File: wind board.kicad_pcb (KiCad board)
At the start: 2 copper layers, 50 x 50 mm, 63 parts, among them J1 USB_C_Receptacle_USB2.0_14P, J2 Conn_01x06_MountingPin, J3 Conn_01x06_MountingPin, U1 CH334R, U2 FT232RL, U3 FT232RL, U4 ZT3222F, U5 ZT3222F, Y1 12MHz

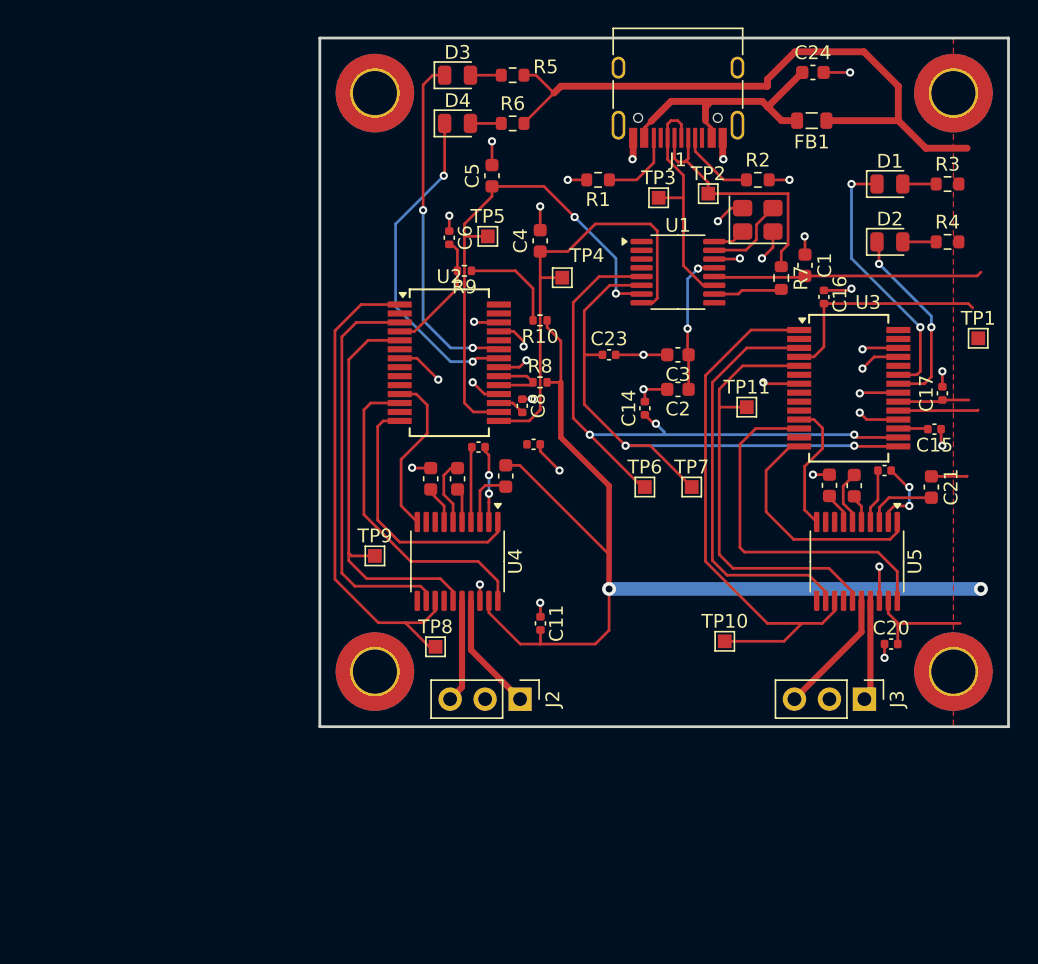
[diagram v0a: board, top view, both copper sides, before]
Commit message: added 3rd interface, tvs diodes, charging circuit
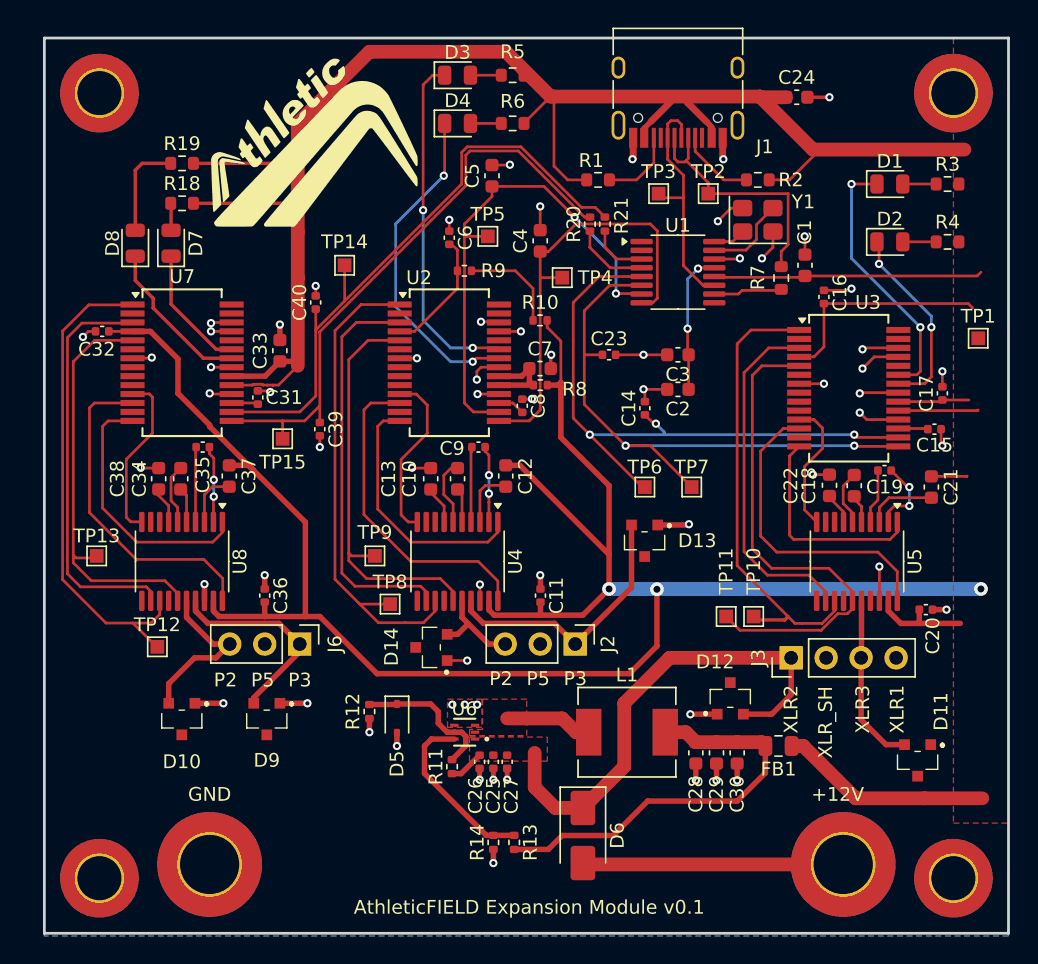
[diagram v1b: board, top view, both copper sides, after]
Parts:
- added C25: 10µF, Capacitor_SMD:C_0402_1005Metric, F.Cu at (131.6, 102.5)
- added C26: 10µF, Capacitor_SMD:C_0402_1005Metric, F.Cu at (130.6, 102.5)
- added C27: 0.1µF, Capacitor_SMD:C_0402_1005Metric, F.Cu at (132.6, 102.5)
- added C28: 22µF, Capacitor_SMD:C_0603_1608Metric, F.Cu at (146.3, 101.9)
- added C29: 22µF, Capacitor_SMD:C_0603_1608Metric, F.Cu at (147.8, 101.9)
- added C30: 22µF, Capacitor_SMD:C_0603_1608Metric, F.Cu at (149.3, 101.9)
- added C31: 100nF, Capacitor_SMD:C_0402_1005Metric, F.Cu at (114.5, 76.1)
- added C32: 100nF, Capacitor_SMD:C_0402_1005Metric, F.Cu at (103.2, 71.3)
- added C33: 4.7µF, Capacitor_SMD:C_0603_1608Metric, F.Cu at (116.1, 72.7)
- added C34: 470nF, Capacitor_SMD:C_0603_1608Metric, F.Cu at (108.9, 82.0)
- added C35: 100nF, Capacitor_SMD:C_0402_1005Metric, F.Cu at (110.5, 79.7)
- added C36: 100nF, Capacitor_SMD:C_0402_1005Metric, F.Cu at (115.0, 90.5)
- added C37: 470nF, Capacitor_SMD:C_0603_1608Metric, F.Cu at (112.4, 81.8)
- added C38: 470nF, Capacitor_SMD:C_0603_1608Metric, F.Cu at (107.3, 82.0)
- added C39: 47pF, Capacitor_SMD:C_0402_1005Metric, F.Cu at (119.0, 78.4)
- added C40: 47pF, Capacitor_SMD:C_0402_1005Metric, F.Cu at (118.7, 69.2)
- added D10: SM15-02HTG, Package_TO_SOT_SMD:SM0502HTG, F.Cu at (109.0, 99.4)
- added D11: SM15-02HTG, Package_TO_SOT_SMD:SM0502HTG, F.Cu at (162.4, 102.4)
- added D12: SM15-02HTG, Package_TO_SOT_SMD:SM0502HTG, F.Cu at (148.8, 97.9)
- added D13: SM15-02HTG, Package_TO_SOT_SMD:SM0502HTG, F.Cu at (142.6, 86.5)
- added D14: SM15-02HTG, Package_TO_SOT_SMD:SM0502HTG, F.Cu at (127.1, 94.2)
- added D5: 1N4148WS, Diode_SMD:D_SOD-323, F.Cu at (124.6, 99.4)
- added D6: SS54, Diode_SMD:D_SMA, F.Cu at (138.1, 107.9)
- added D7: LED, LED_SMD:LED_0805_2012Metric, F.Cu at (108.2, 64.9)
- added D8: LED, LED_SMD:LED_0805_2012Metric, F.Cu at (105.6, 64.9)
- added D9: SM15-02HTG, Package_TO_SOT_SMD:SM0502HTG, F.Cu at (115.2, 99.4)
- added G***: LOGO, logos:athletic Square, F.Cu at (118.6, 57.6)
- added J4: 12V -, MountingHole:MountingHole_4.3mm_M4_ISO7380_Pad_TopBottom, F.Cu at (111.0, 110.0)
- added J5: 12V +, MountingHole:MountingHole_4.3mm_M4_ISO7380_Pad_TopBottom, F.Cu at (157.0, 110.0)
- added J6: Conn_01x06_MountingPin, Connector_PinHeader_2.54mm:PinHeader_1x03_P2.54mm_Vertical, F.Cu at (117.5, 94.0)
- added L1: SPM6530T-2R2M, Inductor_SMD:IND_SPM6530T-2R2M, F.Cu at (141.3, 100.4)
- added R11: 20KΩ, Resistor_SMD:R_0402_1005Metric, F.Cu at (128.6, 102.9)
- added R12: 30KΩ, Resistor_SMD:R_0402_1005Metric, F.Cu at (122.6, 98.9)
- added R13: 220KΩ, Resistor_SMD:R_0402_1005Metric, F.Cu at (133.1, 108.4)
- added R14: 30KΩ, Resistor_SMD:R_0402_1005Metric, F.Cu at (131.6, 108.4)
- added R18: 470Ω, Resistor_SMD:R_0603_1608Metric, F.Cu at (109.0, 62.0)
- added R19: 470Ω, Resistor_SMD:R_0603_1608Metric, F.Cu at (109.0, 59.1)
- added R20: 0Ω, Resistor_SMD:R_0402_1005Metric, F.Cu at (138.6, 63.5)
- added R21: 0Ω, Resistor_SMD:R_0402_1005Metric, F.Cu at (139.7, 63.5)
- added TP12: TestPoint, TestPoint:TestPoint_Pad_1.0x1.0mm, F.Cu at (107.2, 94.2)
- added TP13: TestPoint, TestPoint:TestPoint_Pad_1.0x1.0mm, F.Cu at (102.8, 87.6)
- added TP14: TestPoint, TestPoint:TestPoint_Pad_1.0x1.0mm, F.Cu at (120.8, 66.5)
- added TP15: TestPoint, TestPoint:TestPoint_Pad_1.0x1.0mm, F.Cu at (116.3, 79.1)
- added U6: TPS565242, Package_TO_SOT_SMD:SOT6_DRL_TEX-L, F.Cu at (129.5, 100.4)
- added U7: FT232RL, Package_SO:SSOP-28_5.3x10.2mm_P0.65mm, F.Cu at (109.0, 73.6)
- added U8: ZT3222F, Package_SO:TSSOP-20_4.4x6.5mm_P0.65mm, F.Cu at (109.0, 88.0)
- C7: footprint Capacitor_SMD:C_0402_1005Metric -> Capacitor_SMD:C_0603_1608Metric
- FB1: value 600R/0.5A -> 600R/3A; footprint Inductor_SMD:L_0805_2012Metric -> Capacitor_SMD:C_0805_2012Metric
- J3: footprint Connector_PinHeader_2.54mm:PinHeader_1x03_P2.54mm_Vertical -> Connector_PinHeader_2.54mm:PinHeader_1x04_P2.54mm_Vertical
- R1, R2: value 5.1KΩ -> 22KΩ
- moved FB1 45.5 mm to (152.3, 101.4)
- moved REF** 25.0 mm to (103.0, 111.0)
- moved REF** 20.0 mm to (103.0, 54.0)
- moved TP11 15.3 mm to (148.5, 92.0)
- moved REF** 15.0 mm to (165.0, 111.0)
- moved J3 6.11 mm to (153.2, 95.0), turned to 90 degrees
- moved J2 5.66 mm to (137.5, 94.0)
- moved C7 5.52 mm to (135.0, 74.0)
- moved TP8 4.53 mm to (124.1, 91.1)
- moved C20 3.55 mm to (163.0, 91.5), turned to 180 degrees
- moved TP10 2.77 mm to (150.5, 92.0)
- moved C24 2.15 mm to (153.6, 54.3)
- moved C11 2.02 mm to (135.0, 90.5)
- moved TP3 0.30 mm to (143.6, 61.3)
- moved R8 0.20 mm to (135.0, 75.2)
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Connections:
- net +3.3V renamed Net-(U1-VDD33)
- C24 pad 1: Net-(C24-Pad1) -> +5V
- FB1 pad 2: Net-(C24-Pad1) -> Net-(C28-Pad1)
- J1 pad A4: Net-(C24-Pad1) -> +5V
- J1 pad A9: Net-(C24-Pad1) -> +5V
- J1 pad B4: Net-(C24-Pad1) -> +5V
- J1 pad B9: Net-(C24-Pad1) -> +5V
- J3 pad 1: Net-(J3-Pin_1) -> /WG_+12V
- R1 pad 1: Net-(J1-CC2) -> +5V
- R1 pad 2: ~ -> Net-(J1-CC2)
- R2 pad 1: Net-(J1-CC1) -> +5V
- R2 pad 2: ~ -> Net-(J1-CC1)
- U1 pad 3: unconnected-(U1-DM3--Pad3) -> /DM3-
- U1 pad 4: unconnected-(U1-DP3+-Pad4) -> /DM3+
- U5 pad 17: Net-(J3-Pin_1) -> unconnected-(U5-T1OUT-Pad17)
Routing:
- net +5V: track 178.7 -> 337.9 mm, vias 2 -> 3
- net Net-(U7-USBD-): track 0.00 -> 45.5 mm
- net Net-(U7-USBD+): track 0.00 -> 43.1 mm
- net /WG_+12V: track 0.00 -> 38.3 mm
- net Net-(U7-TXD): track 0.00 -> 35.6 mm
- net Net-(C28-Pad1): track 0.00 -> 30.0 mm
- net Net-(U7-RXD): track 0.00 -> 29.3 mm
- net Net-(U7-RTS): track 0.00 -> 28.5 mm
- net ~: track 68.7 -> 93.0 mm, vias 35 -> 63
- net Net-(U7-CBUS4): track 0.00 -> 24.0 mm
- net Net-(C24-Pad1): track 19.3 -> 0.00 mm
- net Net-(D6-A): track 0.00 -> 18.9 mm
- net Net-(U7-CBUS3): track 0.00 -> 17.7 mm
- net Net-(J6-Pin_1): track 0.00 -> 15.0 mm
- net Net-(U7-CTS): track 0.00 -> 12.9 mm
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- added copper zone on F.Cu, net /WG_+12V
- added copper zone on F.Cu, net Net-(U6-SW)
- added copper zone on F.Cu, net ~
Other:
- board size 50 x 50 mm -> 70 x 65 mm
- board text added: "+12V"
- board text added: "AthleticFIELD Expansion Module v0.1"
- board text added: "GND"
- board text added: "P2"
- board text added: "P3"
- board text added: "P5"
- board text added: "XLR1"
- board text added: "XLR2"
- board text added: "XLR3"
- board text added: "XLR_SH"

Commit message: through hole test points
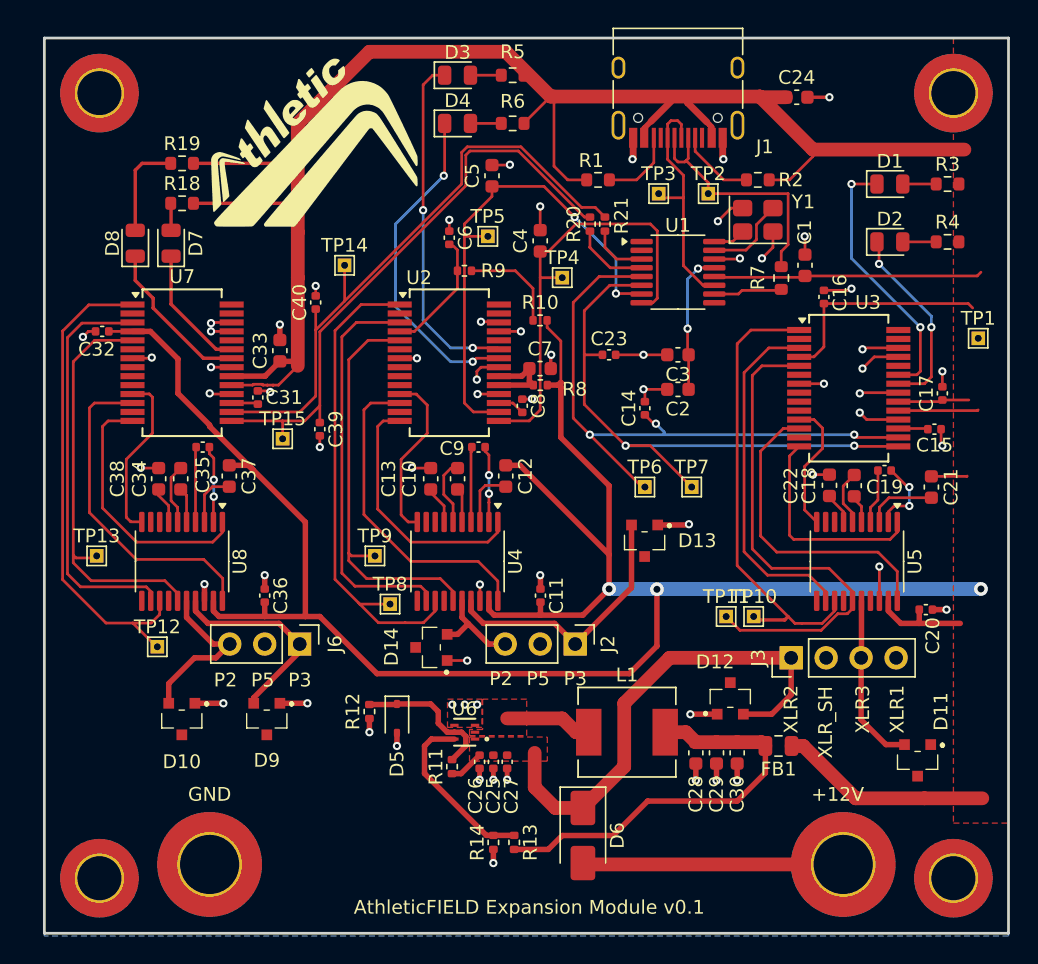
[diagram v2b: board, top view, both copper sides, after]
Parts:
- TP1, TP10, TP11, TP12, TP13, TP14, TP15, TP2, TP3, TP4, TP5, TP6, TP7, TP8, TP9: footprint TestPoint:TestPoint_Pad_1.0x1.0mm -> TestPoint:TestPoint_THTPad_1.0x1.0mm_Drill0.5mm

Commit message: latest
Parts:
- removed R10, R20, R21, R8: 0Ω, Resistor_SMD:R_0402_1005Metric
- added C41: 100nF, Capacitor_SMD:C_0402_1005Metric, F.Cu at (149.9, 111.1)
- added C42: 100nF, Capacitor_SMD:C_0402_1005Metric, F.Cu at (139.1, 110.5)
- added D15: LED, LED_SMD:LED_0805_2012Metric, F.Cu at (109.2, 52.3)
- added G***: LOGO, logos:wind, F.Cu at (122.2, 108.2)
- added G***: LOGO, logos:more_cowbell, B.Cu at (159.9, 101.6)
- added Q1: AONR21321, Transistor_Power_Module:TRANS_AONR21321, F.Cu at (143.4, 109.8)
- C1, C24, C25, C26, C3: value 10µF -> 10uF
- C17, C33, C7: value 4.7µF -> 4.7uF
- C2: value 1µF -> 1uF
- C27: value 0.1µF -> 100nF
- C28, C29, C30: value 22µF -> 22uF
- D6: value SS54 -> MMSZ18T1G; footprint Diode_SMD:D_SMA -> Diode_SMD:D_SOD-123
- FB1: value 600R/3A -> HCB3216KF-601T30; footprint Capacitor_SMD:C_0805_2012Metric -> Capacitor_SMD:C_1206_3216Metric
- R1, R2: value 22KΩ -> 22K
- R11: value 20KΩ -> 20K
- R12, R14: value 30KΩ -> 30K; footprint Resistor_SMD:R_0402_1005Metric -> Resistor_SMD:R_0603_1608Metric
- R13: value 220KΩ -> 220K; footprint Resistor_SMD:R_0402_1005Metric -> Resistor_SMD:R_0603_1608Metric
- R18, R19, R3, R4, R5, R6: value 470Ω -> 470
- R7: value 0 Ω -> 470
- R9: value 0Ω -> 100K
- U2, U3, U7: value FT232RL -> FT232RNL
- moved R9 47.0 mm to (142.5, 112.1)
- moved R7 41.9 mm to (113.5, 52.3), turned to 0 degrees
- moved C6 9.30 mm to (122.9, 72.0), turned to 90 degrees
- moved TP5 6.88 mm to (137.9, 65.8)
- moved C5 6.72 mm to (135.6, 65.3)
- moved TP4 5.46 mm to (131.8, 64.8)
- moved C4 5.23 mm to (129.8, 65.3)
- moved D6 2.66 mm to (137.2, 110.4)
- moved C7 1.37 mm to (133.9, 73.2), turned to 90 degrees
- moved FB1 0.51 mm to (152.8, 101.3)
- moved R13 0.32 mm to (133.1, 108.7)
- moved R14 0.32 mm to (131.6, 108.7)
- moved R12 0.30 mm to (122.6, 99.2)
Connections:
- C14 pad 1: Net-(U1-DM2-) -> Net-(U1-DM1-)
- C23 pad 1: Net-(U1-DP2+) -> Net-(U1-DP1+)
- C39 pad 1: Net-(U7-USBD+) -> /DM3+
- C4 pad 1: Net-(U1-DP1+) -> Net-(U1-DP2+)
- C40 pad 1: Net-(U7-USBD-) -> /DM3-
- C5 pad 1: Net-(U1-DM1-) -> Net-(U1-DM2-)
- C6 pad 2: Net-(U2-VCCIO) -> +5V
- C7 pad 1: Net-(U2-VCC) -> +5V
- J1 pad A7: Net-(J1-D--PadA7) -> Net-(U1-DMU-)
- J1 pad B7: Net-(J1-D--PadA7) -> Net-(U1-DMU-)
- J5 pad 1: Net-(D6-A) -> Net-(J5-Pin_1)
- R7 pad 1: Net-(J1-D--PadA7) -> Net-(D15-A)
- R7 pad 2: Net-(U1-DMU-) -> +5V
- R9 pad 1: Net-(R10-Pad2) -> ~
- R9 pad 2: Net-(U2-VCCIO) -> Net-(D6-A)
- TP14 pad 1: Net-(U7-USBD-) -> /DM3-
- TP15 pad 1: Net-(U7-USBD+) -> /DM3+
- TP2 pad 1: Net-(J1-D--PadA7) -> Net-(U1-DMU-)
- TP4 pad 1: Net-(U1-DP1+) -> Net-(U1-DP2+)
- TP5 pad 1: Net-(U1-DM1-) -> Net-(U1-DM2-)
- TP6 pad 1: Net-(U1-DM2-) -> Net-(U1-DM1-)
- TP7 pad 1: Net-(U1-DP2+) -> Net-(U1-DP1+)
- U2 pad 15: Net-(U1-DP1+) -> Net-(U1-DP2+)
- U2 pad 16: Net-(U1-DM1-) -> Net-(U1-DM2-)
- U2 pad 19: Net-(U2-VCC) -> +5V
- U2 pad 20: Net-(U2-VCC) -> +5V
- U2 pad 4: Net-(U2-VCCIO) -> +5V
- U3 pad 15: Net-(U1-DP2+) -> Net-(U1-DP1+)
- U3 pad 16: Net-(U1-DM2-) -> Net-(U1-DM1-)
- U7 pad 15: Net-(U7-USBD+) -> /DM3+
- U7 pad 16: Net-(U7-USBD-) -> /DM3-
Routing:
- net Net-(U7-USBD-): track 45.5 -> 0.00 mm
- net Net-(U7-USBD+): track 43.1 -> 0.00 mm
- net Net-(J5-Pin_1): track 0.00 -> 41.5 mm
- net /DM3-: track 4.19 -> 43.6 mm
- net /DM3+: track 5.56 -> 42.6 mm
- net +5V: track 337.9 -> 368.8 mm, vias 3 -> 5
- net Net-(J1-D--PadA7): track 19.0 -> 0.00 mm
- net Net-(U1-DM2-): track 46.0 -> 29.5 mm, vias 3 -> 0
- net Net-(U1-DMU-): track 4.97 -> 18.1 mm
- net ~: track 93.0 -> 106.1 mm, vias 63 -> 55
- net Net-(D6-A): track 18.9 -> 6.35 mm
- net Net-(U1-DP2+): track 43.2 -> 31.5 mm
- net Net-(U1-DP1+): track 32.1 -> 42.6 mm, vias 0 -> 2
- net Net-(U1-DM1-): track 36.6 -> 45.5 mm, vias 2 -> 3
- net Net-(U2-VCCIO): track 8.69 -> 0.00 mm
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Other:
- board size 70 x 65 mm -> 70.1 x 65.1 mm
- board text added: "<-- BRIDGE TO RELEASE MAGIC SMOKE -->"
- board text added: "The time has come to act, and act fast! I'm leaving."
- board text added: "XL2"
- board text removed: "XLR2"

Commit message: starting pd chip
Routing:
- net ~: track 106.1 -> 109.2 mm, vias 55 -> 56
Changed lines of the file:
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@@
+	)
+	(segment
+		(start 159.85 72.5)
+		(end 159.6 72.75)
+		(width 0.2)
+		(layer "F.Cu")
+		(net 2)
 	)
 	(segment
@@
 	)
 	(segment
+		(start 159.6 72.75)
+		(end 159.65 72.75)
+		(width 0.2)
+		(layer "F.Cu")
+		(net 2)
+	)
+	(segment
 		(start 122.9 73.3)
 		(end 124.75 73.3)
@@
 	)
 	(segment
+		(start 160 73.15)
+		(end 159.6 72.75)
+		(width 0.2)
+		(layer "F.Cu")
+		(net 2)
+	)
+	(segment
 		(start 142.6 76.4)
 		(end 142.6 75.6)
@@
 	)
 	(segment
+		(start 161 73.15)
+		(end 160 73.15)
+		(width 0.2)
+		(layer "F.Cu")
+		(net 2)
+	)
+	(segment
 		(start 151.9 65.2)
 		(end 151.1 66)
@@
 		(end 133.6 71.3)
 		(width 0.25)
+		(layer "F.Cu")
+		(net 2)
+	)
+	(segment
+		(start 161 72.5)
+		(end 159.85 72.5)
+		(width 0.2)
 		(layer "F.Cu")
 		(net 2)
@@
 		(size 0.6)
 		(drill 0.3)
+		(layers "F.Cu" "B.Cu")
+		(net 2)
+	)
+	(via
+		(at 159.6 72.75)
+		(size 0.6)
+		(drill 0.3)
